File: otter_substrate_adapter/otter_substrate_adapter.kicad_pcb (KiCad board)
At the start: 2 copper layers, 25.4 x 25.4 mm, 18 parts, among them J1 PIX1, J10 R_CONN, J11 PIX1, J12 PIX2, J13 PIX3, J14 BOT_TCE, J15 TOP_TCE, J16 PIX4, J17 PIX5, J18 PIX6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

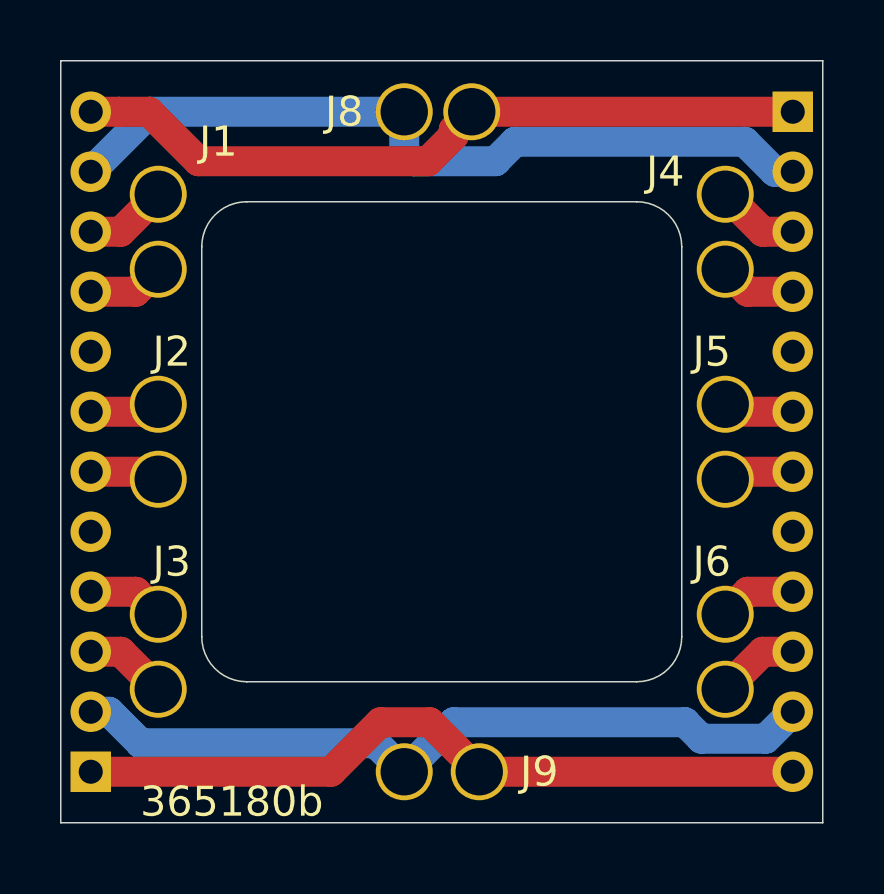
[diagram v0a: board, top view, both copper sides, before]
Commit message: otter crossbars shortened
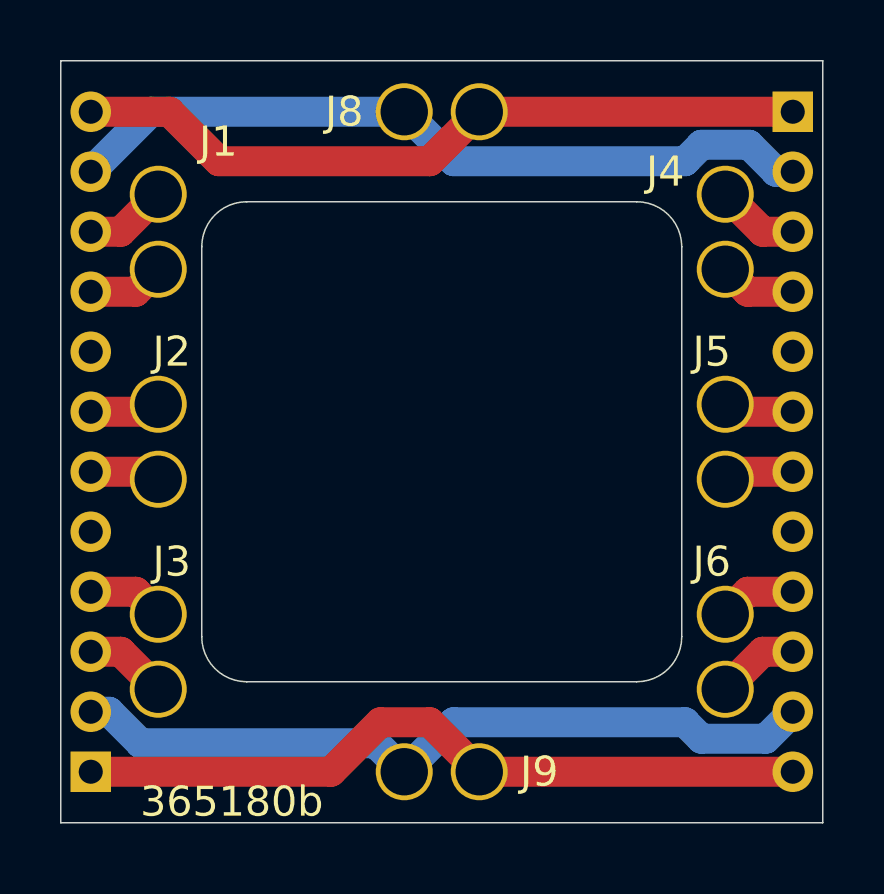
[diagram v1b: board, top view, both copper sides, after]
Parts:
- moved J15 0.25 mm to (1.25, -11.0)
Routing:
- net Net-(J10-Pad2): track 26.4 -> 25.5 mm
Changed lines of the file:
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@@
-(kicad_pcb (version 20171130) (host pcbnew 5.1.5-rc1)
+(kicad_pcb (version 20171130) (host pcbnew 5.1.5)
   (general
     (thickness 1.6)
     (drawings 14)
-    (tracks 57)
+    (tracks 54)
     (zones 0)
     (modules 18)
@@
   )
   (setup
-    (last_trace_width 0.25)
+    (last_trace_width 1)
     (user_trace_width 1)
     (trace_clearance 0.2)
@@
   )
   (module custom:spring_pin (layer F.Cu)
-    (at 1 -11 90)
+    (at 1.25 -11 90)
     (fp_text reference J15 (at 0 2 90) (layer F.SilkS) hide
       (effects (font (size 1 1) (thickness 0.15)))
@@
   (gr_line (start 12.7 12.7) (end 12.7 -12.7) (layer Edge.Cuts) (width 0.05))
   (gr_line (start -12.7 12.7) (end 12.7 12.7) (layer Edge.Cuts) (width 0.05))
-  (segment (start -10.7 -7) (end -9.45 -8.25) (width 1) (layer F.Cu) (net 1))
-  (segment (start -11.7 -7) (end -10.7 -7) (width 1) (layer F.Cu) (net 1))
-  (segment (start -9.7 -1) (end -9.45 -1.25) (width 1) (layer F.Cu) (net 2))
-  (segment (start -11.7 -1) (end -9.7 -1) (width 1) (layer F.Cu) (net 2))
-  (segment (start -10.2 5) (end -9.45 5.75) (width 1) (layer F.Cu) (net 3))
-  (segment (start -11.7 5) (end -10.2 5) (width 1) (layer F.Cu) (net 3))
-  (segment (start 10.7 -7) (end 9.45 -8.25) (width 1) (layer F.Cu) (net 4))
-  (segment (start 11.7 -7) (end 10.7 -7) (width 1) (layer F.Cu) (net 4))
-  (segment (start 9.7 -1) (end 9.45 -1.25) (width 1) (layer F.Cu) (net 5))
-  (segment (start 11.7 -1) (end 9.7 -1) (width 1) (layer F.Cu) (net 5))
-  (segment (start 10.2 5) (end 9.45 5.75) (width 1) (layer F.Cu) (net 6))
-  (segment (start 11.7 5) (end 10.2 5) (width 1) (layer F.Cu) (net 6))
-  (segment (start 11.7 11) (end 1.25 11) (width 1) (layer F.Cu) (net 7))
+  (segment (start -10.7 -7) (end -9.45 -8.25) (width 1) (layer F.Cu) (net 1) (status 20))
+  (segment (start -11.7 -7) (end -10.7 -7) (width 1) (layer F.Cu) (net 1) (status 10))
+  (segment (start -9.7 -1) (end -9.45 -1.25) (width 1) (layer F.Cu) (net 2) (status 30))
+  (segment (start -11.7 -1) (end -9.7 -1) (width 1) (layer F.Cu) (net 2) (status 30))
+  (segment (start -10.2 5) (end -9.45 5.75) (width 1) (layer F.Cu) (net 3) (status 20))
+  (segment (start -11.7 5) (end -10.2 5) (width 1) (layer F.Cu) (net 3) (status 10))
+  (segment (start 10.7 -7) (end 9.45 -8.25) (width 1) (layer F.Cu) (net 4) (status 20))
+  (segment (start 11.7 -7) (end 10.7 -7) (width 1) (layer F.Cu) (net 4) (status 10))
+  (segment (start 9.7 -1) (end 9.45 -1.25) (width 1) (layer F.Cu) (net 5) (status 30))
+  (segment (start 11.7 -1) (end 9.7 -1) (width 1) (layer F.Cu) (net 5) (status 30))
+  (segment (start 10.2 5) (end 9.45 5.75) (width 1) (layer F.Cu) (net 6) (status 20))
+  (segment (start 11.7 5) (end 10.2 5) (width 1) (layer F.Cu) (net 6) (status 10))
+  (segment (start 11.7 11) (end 1.25 11) (width 1) (layer F.Cu) (net 7) (status 30))
   (segment (start -0.400001 9.349999) (end 0.300001 10.050001) (width 1) (layer F.Cu) (net 7))
   (segment (start -3.692002 11) (end -2.042001 9.349999) (width 1) (layer F.Cu) (net 7))
-  (segment (start 0.300001 10.050001) (end 1.25 11) (width 1) (layer F.Cu) (net 7))
+  (segment (start 0.300001 10.050001) (end 1.25 11) (width 1) (layer F.Cu) (net 7) (status 20))
   (segment (start -2.042001 9.349999) (end -0.400001 9.349999) (width 1) (layer F.Cu) (net 7))
-  (segment (start -11.7 11) (end -3.692002 11) (width 1) (layer F.Cu) (net 7))
-  (segment (start 11.025001 9.674999) (end 11.7 9) (width 1) (layer B.Cu) (net 8))
+  (segment (start -11.7 11) (end -3.692002 11) (width 1) (layer F.Cu) (net 7) (status 10))
+  (segment (start 11.025001 9.674999) (end 11.7 9) (width 1) (layer B.Cu) (net 8) (status 20))
   (segment (start 10.799999 9.900001) (end 11.025001 9.674999) (width 1) (layer B.Cu) (net 8))
   (segment (start 8.657999 9.900001) (end 10.799999 9.900001) (width 1) (layer B.Cu) (net 8))
   (segment (start 8.107997 9.349999) (end 8.657999 9.900001) (width 1) (layer B.Cu) (net 8))
   (segment (start 0.400001 9.349999) (end 8.107997 9.349999) (width 1) (layer B.Cu) (net 8))
-  (segment (start -1.25 11) (end 0.400001 9.349999) (width 1) (layer B.Cu) (net 8))
-  (segment (start -11.089998 9) (end -11.7 9) (width 1) (layer B.Cu) (net 8))
-  (segment (start -10.039997 10.050001) (end -11.089998 9) (width 1) (layer B.Cu) (net 8))
+  (segment (start -1.25 11) (end 0.400001 9.349999) (width 1) (layer B.Cu) (net 8) (status 10))
+  (segment (start -11.089998 9) (end -11.7 9) (width 1) (layer B.Cu) (net 8) (status 30))
+  (segment (start -10.039997 10.050001) (end -11.089998 9) (width 1) (layer B.Cu) (net 8) (status 20))
   (segment (start -2.199999 10.050001) (end -10.039997 10.050001) (width 1) (layer B.Cu) (net 8))
-  (segment (start -1.25 11) (end -2.199999 10.050001) (width 1) (layer B.Cu) (net 8))
-  (segment (start -10.7 7) (end -9.45 8.25) (width 1) (layer F.Cu) (net 9))
-  (segment (start -11.7 7) (end -10.7 7) (width 1) (layer F.Cu) (net 9))
-  (segment (start -9.7 1) (end -9.45 1.25) (width 1) (layer F.Cu) (net 10))
-  (segment (start -11.7 1) (end -9.7 1) (width 1) (layer F.Cu) (net 10))
-  (segment (start -10.2 -5) (end -9.45 -5.75) (width 1) (layer F.Cu) (net 11))
-  (segment (start -11.7 -5) (end -10.2 -5) (width 1) (layer F.Cu) (net 11))
-  (segment (start -9.7 -11) (end -1.25 -11) (width 1) (layer B.Cu) (net 12))
-  (segment (start -11.7 -9) (end -9.7 -11) (width 1) (layer B.Cu) (net 12))
-  (segment (start -0.943501 -9.349999) (end -1.25 -9.656498) (width 1) (layer B.Cu) (net 12))
-  (segment (start 1.792001 -9.349999) (end -0.943501 -9.349999) (width 1) (layer B.Cu) (net 12))
-  (segment (start 2.442002 -10) (end 1.792001 -9.349999) (width 1) (layer B.Cu) (net 12))
-  (segment (start -1.25 -9.656498) (end -1.25 -11) (width 1) (layer B.Cu) (net 12))
-  (segment (start 10.100001 -10) (end 2.442002 -10) (width 1) (layer B.Cu) (net 12))
-  (segment (start 11.100001 -9) (end 10.100001 -10) (width 1) (layer B.Cu) (net 12))
-  (segment (start 11.7 -9) (end 11.100001 -9) (width 1) (layer B.Cu) (net 12))
-  (segment (start 11.7 -11) (end 1 -11) (width 1) (layer F.Cu) (net 13))
-  (segment (start -0.457999 -9.349999) (end -8.107997 -9.349999) (width 1) (layer F.Cu) (net 13))
-  (segment (start -9.757998 -11) (end -10.745406 -11) (width 1) (layer F.Cu) (net 13))
-  (segment (start -8.107997 -9.349999) (end -9.757998 -11) (width 1) (layer F.Cu) (net 13))
-  (segment (start 0.400001 -10.207999) (end -0.457999 -9.349999) (width 1) (layer F.Cu) (net 13))
-  (segment (start 0.400001 -10.400001) (end 0.400001 -10.207999) (width 1) (layer F.Cu) (net 13))
-  (segment (start -10.745406 -11) (end -11.7 -11) (width 1) (layer F.Cu) (net 13))
-  (segment (start 1 -11) (end 0.400001 -10.400001) (width 1) (layer F.Cu) (net 13))
-  (segment (start 10.7 7) (end 9.45 8.25) (width 1) (layer F.Cu) (net 14))
-  (segment (start 11.7 7) (end 10.7 7) (width 1) (layer F.Cu) (net 14))
-  (segment (start 9.7 1) (end 9.45 1.25) (width 1) (layer F.Cu) (net 15))
-  (segment (start 11.7 1) (end 9.7 1) (width 1) (layer F.Cu) (net 15))
-  (segment (start 10.2 -5) (end 9.45 -5.75) (width 1) (layer F.Cu) (net 16))
-  (segment (start 11.7 -5) (end 10.2 -5) (width 1) (layer F.Cu) (net 16))
+  (segment (start -1.25 11) (end -2.199999 10.050001) (width 1) (layer B.Cu) (net 8) (status 10))
+  (segment (start -10.7 7) (end -9.45 8.25) (width 1) (layer F.Cu) (net 9) (status 20))
+  (segment (start -11.7 7) (end -10.7 7) (width 1) (layer F.Cu) (net 9) (status 10))
+  (segment (start -9.7 1) (end -9.45 1.25) (width 1) (layer F.Cu) (net 10) (status 30))
+  (segment (start -11.7 1) (end -9.7 1) (width 1) (layer F.Cu) (net 10) (status 30))
+  (segment (start -10.2 -5) (end -9.45 -5.75) (width 1) (layer F.Cu) (net 11) (status 20))
+  (segment (start -11.7 -5) (end -10.2 -5) (width 1) (layer F.Cu) (net 11) (status 10))
+  (segment (start -9.7 -11) (end -1.25 -11) (width 1) (layer B.Cu) (net 12) (status 20))
+  (segment (start -11.7 -9) (end -9.7 -11) (width 1) (layer B.Cu) (net 12) (status 10))
+  (segment (start 0.400001 -9.349999) (end 8.107997 -9.349999) (width 1) (layer B.Cu) (net 12))
+  (segment (start -1.25 -11) (end 0.400001 -9.349999) (width 1) (layer B.Cu) (net 12))
+  (segment (start 8.107997 -9.349999) (end 8.657999 -9.900001) (width 1) (layer B.Cu) (net 12))
+  (segment (start 11.142002 -9) (end 11.7 -9) (width 1) (layer B.Cu) (net 12))
+  (segment (start 10.242001 -9.900001) (end 11.142002 -9) (width 1) (layer B.Cu) (net 12))
+  (segment (start 8.657999 -9.900001) (end 10.242001 -9.900001) (width 1) (layer B.Cu) (net 12))
+  (segment (start 0.300001 -10.050001) (end 1.25 -11) (width 1) (layer F.Cu) (net 13) (status 20))
+  (segment (start -7.425297 -9.349999) (end -0.400001 -9.349999) (width 1) (layer F.Cu) (net 13))
+  (segment (start -9.075298 -11) (end -7.425297 -9.349999) (width 1) (layer F.Cu) (net 13))
+  (segment (start -0.400001 -9.349999) (end 0.300001 -10.050001) (width 1) (layer F.Cu) (net 13))
+  (segment (start -11.7 -11) (end -9.075298 -11) (width 1) (layer F.Cu) (net 13) (status 10))
+  (segment (start 1.25 -11) (end 11.7 -11) (width 1) (layer F.Cu) (net 13) (status 30))
+  (segment (start 10.7 7) (end 9.45 8.25) (width 1) (layer F.Cu) (net 14) (status 20))
+  (segment (start 11.7 7) (end 10.7 7) (width 1) (layer F.Cu) (net 14) (status 10))
+  (segment (start 9.7 1) (end 9.45 1.25) (width 1) (layer F.Cu) (net 15) (status 30))
+  (segment (start 11.7 1) (end 9.7 1) (width 1) (layer F.Cu) (net 15) (status 30))
+  (segment (start 10.2 -5) (end 9.45 -5.75) (width 1) (layer F.Cu) (net 16) (status 20))
+  (segment (start 11.7 -5) (end 10.2 -5) (width 1) (layer F.Cu) (net 16) (status 10))
 )

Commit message: update silk
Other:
- board text added: "6c4861d"
- board text removed: "365180b"
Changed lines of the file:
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@@
   )
   (setup
-    (last_trace_width 1)
+    (last_trace_width 0.25)
     (user_trace_width 1)
     (trace_clearance 0.2)
@@
       (effects (font (size 1 1) (thickness 0.15)))
     )
-    (pad 1 thru_hole circle (at 0 0 90) (size 1.9 1.9) (drill 1.58) (layers *.Cu *.Mask)
+    (pad 1 thru_hole circle (at 0 0 90) (size 1.9 1.9) (drill 1.56) (layers *.Cu *.Mask)
       (net 1 "Net-(J1-Pad1)"))
     (model ${KIPRJMOD}/../3d/mill-max-0964-0-15-20-85-14-11-0.step
@@
       (effects (font (size 1 1) (thickness 0.15)))
     )
-    (pad 1 thru_hole circle (at 0 0 90) (size 1.9 1.9) (drill 1.58) (layers *.Cu *.Mask)
+    (pad 1 thru_hole circle (at 0 0 90) (size 1.9 1.9) (drill 1.56) (layers *.Cu *.Mask)
       (net 2 "Net-(J2-Pad1)"))
     (model ${KIPRJMOD}/../3d/mill-max-0964-0-15-20-85-14-11-0.step
@@
       (effects (font (size 1 1) (thickness 0.15)))
     )
-    (pad 1 thru_hole circle (at 0 0 90) (size 1.9 1.9) (drill 1.58) (layers *.Cu *.Mask)
+    (pad 1 thru_hole circle (at 0 0 90) (size 1.9 1.9) (drill 1.56) (layers *.Cu *.Mask)
       (net 3 "Net-(J3-Pad1)"))
     (model ${KIPRJMOD}/../3d/mill-max-0964-0-15-20-85-14-11-0.step
@@
       (effects (font (size 1 1) (thickness 0.15)))
     )
-    (pad 1 thru_hole circle (at 0 0 90) (size 1.9 1.9) (drill 1.58) (layers *.Cu *.Mask)
+    (pad 1 thru_hole circle (at 0 0 90) (size 1.9 1.9) (drill 1.56) (layers *.Cu *.Mask)
       (net 4 "Net-(J10-Pad3)"))
     (model ${KIPRJMOD}/../3d/mill-max-0964-0-15-20-85-14-11-0.step
@@
       (effects (font (size 1 1) (thickness 0.15)))
     )
-    (pad 1 thru_hole circle (at 0 0 90) (size 1.9 1.9) (drill 1.58) (layers *.Cu *.Mask)
+    (pad 1 thru_hole circle (at 0 0 90) (size 1.9 1.9) (drill 1.56) (layers *.Cu *.Mask)
       (net 5 "Net-(J10-Pad6)"))
     (model ${KIPRJMOD}/../3d/mill-max-0964-0-15-20-85-14-11-0.step
@@
       (effects (font (size 1 1) (thickness 0.15)))
     )
-    (pad 1 thru_hole circle (at 0 0 90) (size 1.9 1.9) (drill 1.58) (layers *.Cu *.Mask)
+    (pad 1 thru_hole circle (at 0 0 90) (size 1.9 1.9) (drill 1.56) (layers *.Cu *.Mask)
       (net 6 "Net-(J10-Pad9)"))
     (model ${KIPRJMOD}/../3d/mill-max-0964-0-15-20-85-14-11-0.step
@@
       (effects (font (size 1 1) (thickness 0.15)))
     )
-    (pad 1 thru_hole circle (at 0 0 90) (size 1.9 1.9) (drill 1.58) (layers *.Cu *.Mask)
+    (pad 1 thru_hole circle (at 0 0 90) (size 1.9 1.9) (drill 1.56) (layers *.Cu *.Mask)
       (net 12 "Net-(J10-Pad2)"))
     (model ${KIPRJMOD}/../3d/mill-max-0964-0-15-20-85-14-11-0.step
@@
       (effects (font (size 1 1) (thickness 0.15)))
     )
-    (pad 1 thru_hole circle (at 0 0 90) (size 1.9 1.9) (drill 1.58) (layers *.Cu *.Mask)
+    (pad 1 thru_hole circle (at 0 0 90) (size 1.9 1.9) (drill 1.56) (layers *.Cu *.Mask)
       (net 7 "Net-(J10-Pad12)"))
     (model ${KIPRJMOD}/../3d/mill-max-0964-0-15-20-85-14-11-0.step
@@
       (effects (font (size 1 1) (thickness 0.15)))
     )
-    (pad 1 thru_hole circle (at 0 0 90) (size 1.9 1.9) (drill 1.58) (layers *.Cu *.Mask)
+    (pad 1 thru_hole circle (at 0 0 90) (size 1.9 1.9) (drill 1.56) (layers *.Cu *.Mask)
       (net 11 "Net-(J11-Pad1)"))
     (model ${KIPRJMOD}/../3d/mill-max-0964-0-15-20-85-14-11-0.step
@@
       (effects (font (size 1 1) (thickness 0.15)))
     )
-    (pad 1 thru_hole circle (at 0 0 90) (size 1.9 1.9) (drill 1.58) (layers *.Cu *.Mask)
+    (pad 1 thru_hole circle (at 0 0 90) (size 1.9 1.9) (drill 1.56) (layers *.Cu *.Mask)
       (net 10 "Net-(J12-Pad1)"))
     (model ${KIPRJMOD}/../3d/mill-max-0964-0-15-20-85-14-11-0.step
@@
       (effects (font (size 1 1) (thickness 0.15)))
     )
-    (pad 1 thru_hole circle (at 0 0 90) (size 1.9 1.9) (drill 1.58) (layers *.Cu *.Mask)
+    (pad 1 thru_hole circle (at 0 0 90) (size 1.9 1.9) (drill 1.56) (layers *.Cu *.Mask)
       (net 9 "Net-(J13-Pad1)"))
     (model ${KIPRJMOD}/../3d/mill-max-0964-0-15-20-85-14-11-0.step
@@
       (effects (font (size 1 1) (thickness 0.15)))
     )
-    (pad 1 thru_hole circle (at 0 0 90) (size 1.9 1.9) (drill 1.58) (layers *.Cu *.Mask)
+    (pad 1 thru_hole circle (at 0 0 90) (size 1.9 1.9) (drill 1.56) (layers *.Cu *.Mask)
       (net 8 "Net-(J10-Pad11)"))
     (model ${KIPRJMOD}/../3d/mill-max-0964-0-15-20-85-14-11-0.step
@@
       (effects (font (size 1 1) (thickness 0.15)))
     )
-    (pad 1 thru_hole circle (at 0 0 90) (size 1.9 1.9) (drill 1.58) (layers *.Cu *.Mask)
+    (pad 1 thru_hole circle (at 0 0 90) (size 1.9 1.9) (drill 1.56) (layers *.Cu *.Mask)
       (net 13 "Net-(J10-Pad1)"))
     (model ${KIPRJMOD}/../3d/mill-max-0964-0-15-20-85-14-11-0.step
@@
       (effects (font (size 1 1) (thickness 0.15)))
     )
-    (pad 1 thru_hole circle (at 0 0 90) (size 1.9 1.9) (drill 1.58) (layers *.Cu *.Mask)
+    (pad 1 thru_hole circle (at 0 0 90) (size 1.9 1.9) (drill 1.56) (layers *.Cu *.Mask)
       (net 16 "Net-(J10-Pad4)"))
     (model ${KIPRJMOD}/../3d/mill-max-0964-0-15-20-85-14-11-0.step
@@
       (effects (font (size 1 1) (thickness 0.15)))
     )
-    (pad 1 thru_hole circle (at 0 0 90) (size 1.9 1.9) (drill 1.58) (layers *.Cu *.Mask)
+    (pad 1 thru_hole circle (at 0 0 90) (size 1.9 1.9) (drill 1.56) (layers *.Cu *.Mask)
       (net 15 "Net-(J10-Pad7)"))
     (model ${KIPRJMOD}/../3d/mill-max-0964-0-15-20-85-14-11-0.step
@@
       (effects (font (size 1 1) (thickness 0.15)))
     )
-    (pad 1 thru_hole circle (at 0 0 90) (size 1.9 1.9) (drill 1.58) (layers *.Cu *.Mask)
+    (pad 1 thru_hole circle (at 0 0 90) (size 1.9 1.9) (drill 1.56) (layers *.Cu *.Mask)
       (net 14 "Net-(J10-Pad10)"))
     (model ${KIPRJMOD}/../3d/mill-max-0964-0-15-20-85-14-11-0.step
@@
   (gr_arc (start -6.5 6.5) (end -8 6.5) (angle -90) (layer Edge.Cuts) (width 0.05))
   (gr_arc (start 6.5 6.5) (end 6.5 8) (angle -90) (layer Edge.Cuts) (width 0.05))
-  (gr_text 365180b (at -7 12) (layer B.SilkS)
+  (gr_text 6c4861d (at -7 12) (layer B.SilkS)
     (effects (font (size 1 1) (thickness 0.15)) (justify mirror))
   )
-  (gr_text 365180b (at -7 12) (layer F.SilkS)
+  (gr_text 6c4861d (at -7 12) (layer F.SilkS)
     (effects (font (size 1 1) (thickness 0.15)))
   )
